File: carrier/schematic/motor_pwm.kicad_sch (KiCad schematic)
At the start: 9 parts, among them J36001 HX PZ2.54-3x8P ZZ, U36001 SN74HCT245PWR, U36003 SY6280AAC

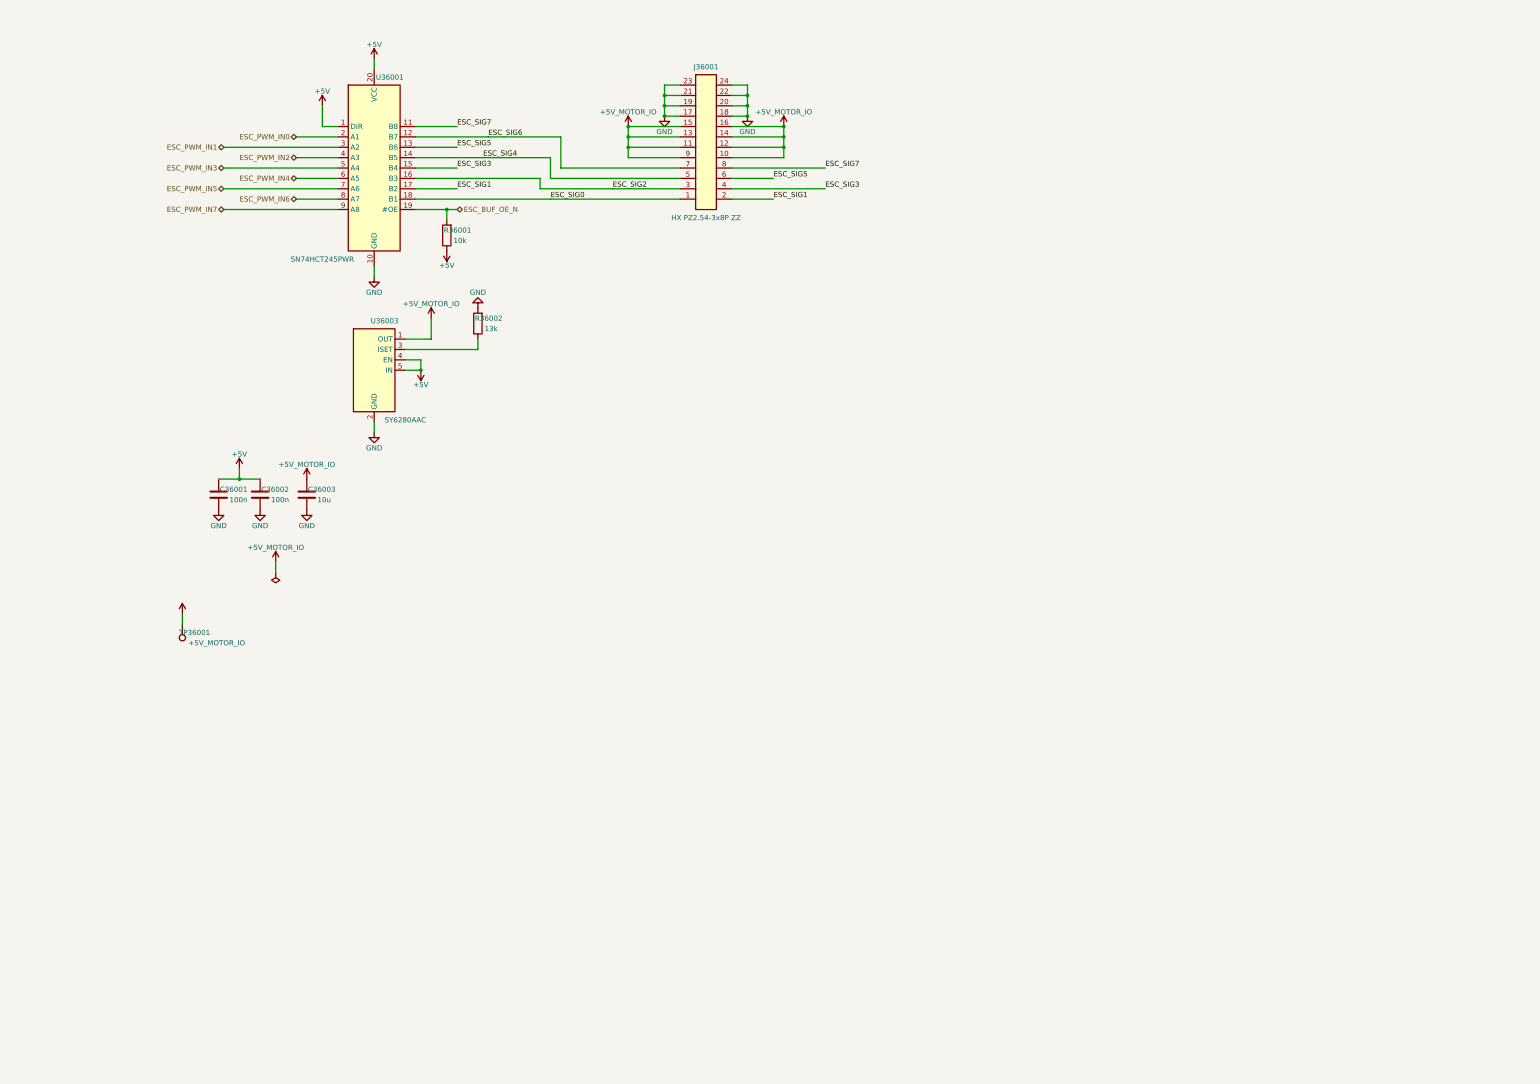
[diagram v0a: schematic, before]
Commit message: feat(motor_pwm LAW-7): instantiate the 33R output series-damping (placer row-wrap)
The 33R per-channel series damping on the 8 buffered ESC outputs was held back in
the prior commit (doc-tracked) because the part C25508 (4D03WGJ0330T5E 4x33R
array) is sourced but two 4-element arrays reconverging on the 24-pin header form
a tree the per-sheet chain placer strung to >400mm (over A3). LAW 7 says land a
sourced fix, not defer it — so this lands it:

 * motor_pwm.py: U1.B{i} -> RN(33R).in -> RN.out -> J1.SIG{1+i}; two isolated
   4D03 arrays (RN1 ch0-3, RN2 ch4-7), element j spanning pin (j+1)<->(8-j) per
   the footprint's vertical pad pairs. ISOLATED elements (no internal common) so
   a faulted ESC lead can't back-feed a sibling.
 * place.py: a within-component ROW-WRAP in _chain_template (PAPER_W_BUDGET=330).
   The discriminator is the POST-placement anchor (ax - row_left), NOT the prior
   attempt's pre-placement run-width that wrongly tripped lcd. Instrumented:
   widest FITTING sheet = lcd 292.7mm, overflowing motor_pwm = 370.1mm, so 330
   is a clean separator -> ONLY motor_pwm wraps. Proven byte-identical: of all 37
   sheets only motor_pwm.kicad_sch changed (lcd/hdmi_rx/all others identical).

The wrap demotes the crossed channel to labeled stubs (KiCad merges by name,
netlist untouched). BOARD PASS (159x145mm, 561 fp), DRC 0, LINK 0, CC-gate 0
shorts/0 opens, ratsnest/spacing/power-tree green; motor_pwm 8 local tests pass.
Only the 5V-rated output ESD array remains deferred (API-blocked — a 3.3V array
would clamp the 5V PWM).

Co-Authored-By: Claude Opus 4.8 <noreply@anthropic.com>
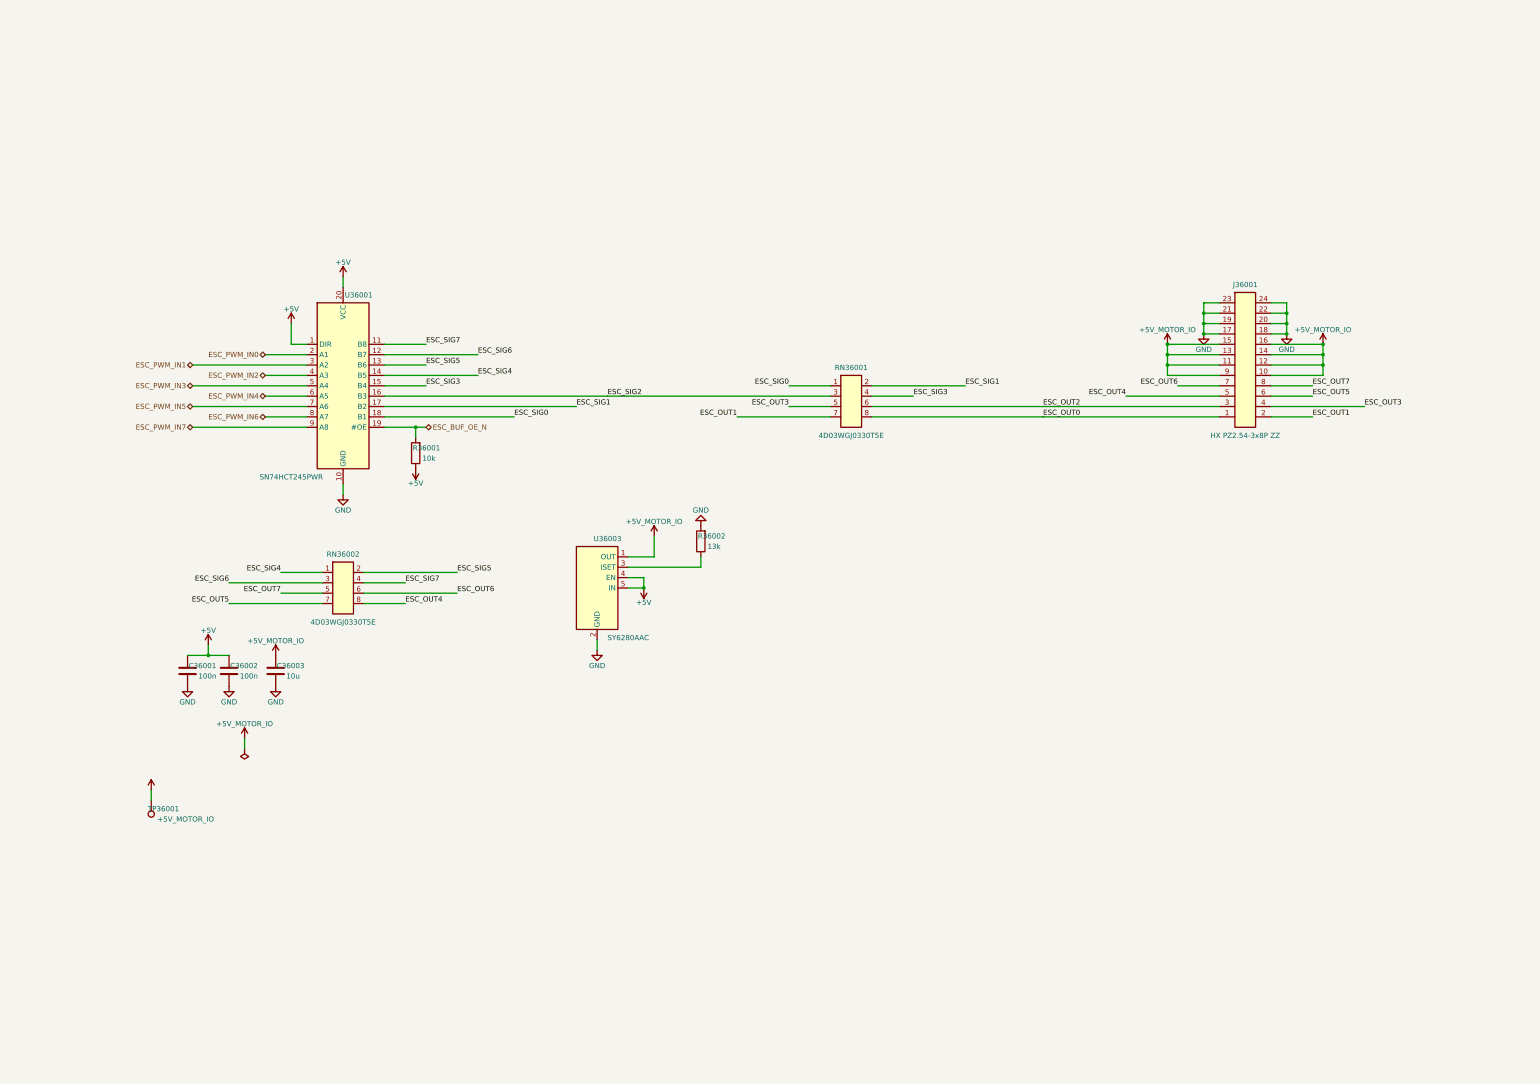
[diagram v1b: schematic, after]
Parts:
- added C36003: 10u, Capacitor_SMD:C_0805_2012Metric, symbol Device:C
- added TP36001: +5V_MOTOR_IO, TestPoint:TestPoint_Pad_D1.5mm, symbol Connector:TestPoint
- C36001: renamed from C36003; value 10u -> 100n; footprint Capacitor_SMD:C_0805_2012Metric -> Capacitor_SMD:C_0603_1608Metric; LCSC C15850 -> C14663
- C36002: renamed from TP36001; value +5V_MOTOR_IO -> 100n; footprint TestPoint:TestPoint_Pad_D1.5mm -> Capacitor_SMD:C_0603_1608Metric; symbol Connector:TestPoint -> Device:C; BOM exclude -> (none); LCSC (none) -> C14663
- J36001: renamed from U36003; value SY6280AAC -> HX PZ2.54-3x8P ZZ; footprint SY6280AAC:SY6280AAC -> HX_PZ2.54-3x8P_ZZ:HX_PZ2.54-3x8P_ZZ; symbol SY6280AAC:SY6280AAC -> HX_PZ2.54-3x8P_ZZ:HX_PZ2.54-3x8P_ZZ; LCSC C55136 -> C32713295
- R36002: renamed from C36002; value 100n -> 13k; footprint Capacitor_SMD:C_0603_1608Metric -> Resistor_SMD:R_0603_1608Metric; symbol Device:C -> Device:R; LCSC C14663 -> C22797
- RN36001: renamed from J36001; value HX PZ2.54-3x8P ZZ -> 4D03WGJ0330T5E; footprint HX_PZ2.54-3x8P_ZZ:HX_PZ2.54-3x8P_ZZ -> 4D03WGJ0330T5E:4D03WGJ0330T5E; symbol HX_PZ2.54-3x8P_ZZ:HX_PZ2.54-3x8P_ZZ -> 4D03WGJ0330T5E:4D03WGJ0330T5E; LCSC C32713295 -> C25508
- RN36002: renamed from R36002; value 13k -> 4D03WGJ0330T5E; footprint Resistor_SMD:R_0603_1608Metric -> 4D03WGJ0330T5E:4D03WGJ0330T5E; symbol Device:R -> 4D03WGJ0330T5E:4D03WGJ0330T5E; LCSC C22797 -> C25508
- U36003: renamed from C36001; value 100n -> SY6280AAC; footprint Capacitor_SMD:C_0603_1608Metric -> SY6280AAC:SY6280AAC; symbol Device:C -> SY6280AAC:SY6280AAC; LCSC C14663 -> C55136
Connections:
- net +5V: now also C36001.1, C36002.1, U36003.4 (EN), U36003.5 (IN); no longer J36001.4 (EN), J36001.5 (IN), R36002.1, U36003.1
- net +5V_MOTOR_IO: now also J36001.10, J36001.11, J36001.12, J36001.13, J36001.14, J36001.15, J36001.16, J36001.9, U36003.1 (OUT), C36003.1, TP36001.1; no longer C36001.1, C36002.1, J36001.1 (OUT), RN36001.10, RN36001.11, RN36001.12, RN36001.13, RN36001.14, RN36001.15, RN36001.16, RN36001.9
- net ESC_SIG4: now also RN36002.1; no longer RN36001.5
- net ESC_SIG5: now also RN36002.2; no longer RN36001.6
- net ESC_SIG6: now also RN36002.3; no longer RN36001.7
- net ESC_SIG7: now also RN36002.4; no longer RN36001.8
- net GND: now also C36002.2, J36001.17, J36001.18, J36001.19, J36001.20, J36001.21, J36001.22, J36001.23, J36001.24, C36003.2; no longer J36001.2 (GND), RN36001.17, RN36001.18, RN36001.19, RN36001.20, RN36001.21, RN36001.22, RN36001.23, RN36001.24, RN36002.2
- net ESC_OUT2: now reaches J36001.3
- net ESC_OUT2: now also RN36001.6; no longer RN36002.1
- new net: R36002.1, U36003.3 (ISET)
- new net ESC_OUT0: J36001.1, RN36001.8
- new net ESC_OUT1: J36001.2, RN36001.7
- new net ESC_OUT3: J36001.4, RN36001.5
- new net ESC_OUT4: J36001.5, RN36002.8
- new net ESC_OUT5: J36001.6, RN36002.7
- new net ESC_OUT6: J36001.7, RN36002.6
- new net ESC_OUT7: J36001.8, RN36002.5
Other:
- moved on the sheet: C36001, R36001, U36001

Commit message: feat(motor_pwm OPEN-3a): 5V-rated ESD on the 8 off-board PWM outputs
Lands the long-deferred output ESD — NO EasyEDA CAD API needed (it was rate-
limited): SRV05-4 is a jellybean part with a STOCK KiCad symbol
(Power_Protection:SRV05-4, pinout built-in) + stock SOT-23-6 footprint; the
verified LCSC C2836319 (MSKSEMI SRV05-4, 375k stock) rides in the value + a
ratings.py line.

Two arrays clamp ESC_OUT0..7 to +5V/GND right at the connector, ahead of the 33R
+ buffer. SRV05-4 is 5V-line rated, so unlike the spec's 3.3V PESD3V3L4UG it does
NOT clamp the 5V buffered signals. Bound by pad NUMBER (schgen resolves pins by
number): IO1=1/VN=2/IO2=3/IO3=4/VP=5/IO4=6 -> VP->+5V, VN->GND, the 4 I/O ->
4 channels each. The taps distribute across 8 separate ESC_OUT nets, so (unlike
the motor_sense bulk cap on one dense net) the schematic router took it with no
congestion. D36001/D36002 placed clean below the buffer (render-verified, refs
0-overlap per the LAW-1 gate).

PART RULES PASS (C2836319 = diode v_max 5.0), DRC 0, 564 footprints, motor_pwm
8 tests + full suite 662 passed. OPEN-3: (a) ESD + (b) bulk cap now both landed;
(c) shunt remains a design decision (aggregate-current sizing + INA range).

Co-Authored-By: Claude Opus 4.8 <noreply@anthropic.com>
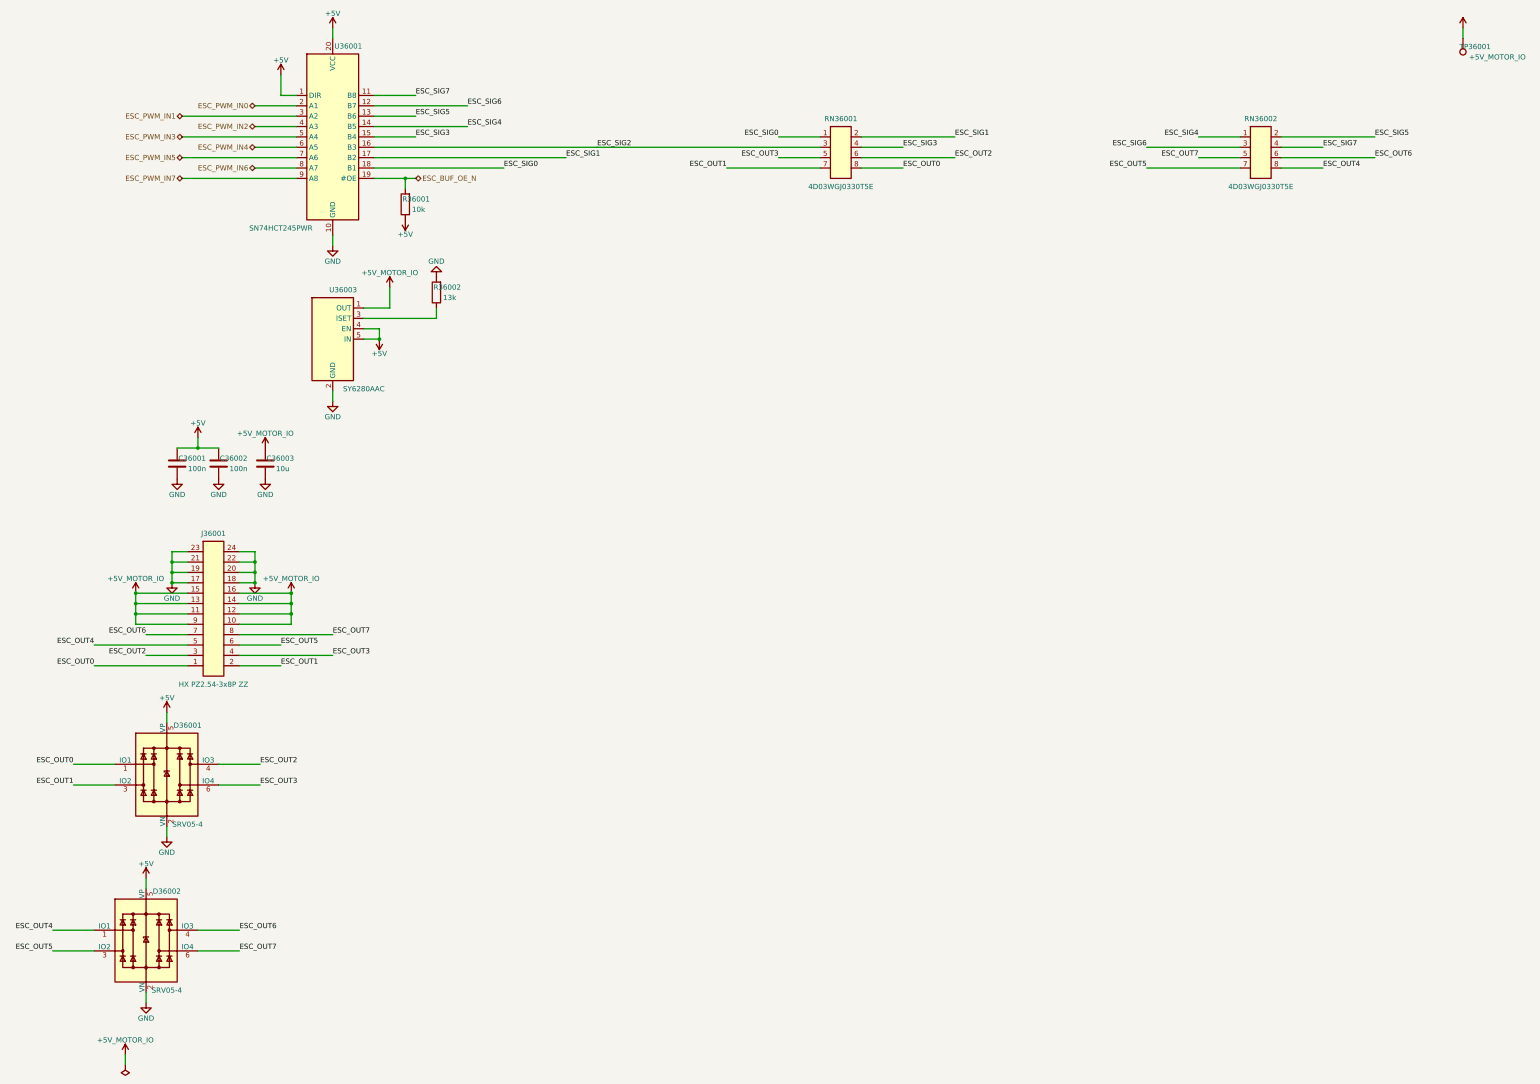
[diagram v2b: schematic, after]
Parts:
- added D36002: SRV05-4, Package_TO_SOT_SMD:SOT-23-6, symbol Power_Protection:SRV05-4
- added TP36001: +5V_MOTOR_IO, TestPoint:TestPoint_Pad_D1.5mm, symbol Connector:TestPoint
- C36001: renamed from R36002; value 13k -> 100n; footprint Resistor_SMD:R_0603_1608Metric -> Capacitor_SMD:C_0603_1608Metric; symbol Device:R -> Device:C; LCSC C22797 -> C14663
- C36003: renamed from C36002; value 100n -> 10u; footprint Capacitor_SMD:C_0603_1608Metric -> Capacitor_SMD:C_0805_2012Metric; LCSC C14663 -> C15850
- D36001: renamed from TP36001; value +5V_MOTOR_IO -> SRV05-4; footprint TestPoint:TestPoint_Pad_D1.5mm -> Package_TO_SOT_SMD:SOT-23-6; symbol Connector:TestPoint -> Power_Protection:SRV05-4; BOM exclude -> (none); LCSC (none) -> C2836319
- J36001: renamed from C36003; value 10u -> HX PZ2.54-3x8P ZZ; footprint Capacitor_SMD:C_0805_2012Metric -> HX_PZ2.54-3x8P_ZZ:HX_PZ2.54-3x8P_ZZ; symbol Device:C -> HX_PZ2.54-3x8P_ZZ:HX_PZ2.54-3x8P_ZZ; LCSC C15850 -> C32713295
- R36002: renamed from U36003; value SY6280AAC -> 13k; footprint SY6280AAC:SY6280AAC -> Resistor_SMD:R_0603_1608Metric; symbol SY6280AAC:SY6280AAC -> Device:R; LCSC C55136 -> C22797
- RN36002: renamed from J36001; value HX PZ2.54-3x8P ZZ -> 4D03WGJ0330T5E; footprint HX_PZ2.54-3x8P_ZZ:HX_PZ2.54-3x8P_ZZ -> 4D03WGJ0330T5E:4D03WGJ0330T5E; symbol HX_PZ2.54-3x8P_ZZ:HX_PZ2.54-3x8P_ZZ -> 4D03WGJ0330T5E:4D03WGJ0330T5E; LCSC C32713295 -> C25508
- U36003: renamed from RN36002; value 4D03WGJ0330T5E -> SY6280AAC; footprint 4D03WGJ0330T5E:4D03WGJ0330T5E -> SY6280AAC:SY6280AAC; symbol 4D03WGJ0330T5E:4D03WGJ0330T5E -> SY6280AAC:SY6280AAC; LCSC C25508 -> C55136
- renumbered C36001 to C36002
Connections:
- net +5V: now also C36001.1, D36001.5 (VP), U36003.4 (EN), U36003.5 (IN), D36002.5 (VP); no longer C36003.1, R36002.4 (EN), R36002.5 (IN)
- net +5V_MOTOR_IO: now also C36003.1, J36001.10, J36001.11, J36001.12, J36001.13, J36001.14, J36001.15, J36001.16, J36001.9, U36003.1 (OUT), TP36001.1; no longer D36001.1, J36001.1, R36002.1 (OUT), RN36002.10, RN36002.11, RN36002.12, RN36002.13, RN36002.14, RN36002.15, RN36002.16, RN36002.9
- net ESC_OUT0: now also D36001.1 (IO1), J36001.1; no longer RN36002.1
- net ESC_OUT1: now also D36001.3 (IO2), J36001.2; no longer RN36002.2
- net ESC_OUT2: now also D36001.4 (IO3), J36001.3; no longer RN36002.3
- net ESC_OUT3: now also D36001.6 (IO4), J36001.4; no longer RN36002.4
- net ESC_OUT4: now also J36001.5, RN36002.8, D36002.1 (IO1); no longer RN36002.5, U36003.8
- net ESC_OUT5: now also J36001.6, RN36002.7, D36002.3 (IO2); no longer RN36002.6, U36003.7
- net ESC_OUT6: now also J36001.7, RN36002.6, D36002.4 (IO3); no longer RN36002.7, U36003.6
- net ESC_OUT7: now also J36001.8, RN36002.5, D36002.6 (IO4); no longer RN36002.8, U36003.5
- net ESC_SIG4: now also RN36002.1; no longer U36003.1
- net ESC_SIG5: now also RN36002.2; no longer U36003.2
- net ESC_SIG6: now also RN36002.3; no longer U36003.3
- net ESC_SIG7: now also RN36002.4; no longer U36003.4
- net GND: now also D36001.2 (VN), J36001.17, J36001.18, J36001.19, J36001.20, J36001.21, J36001.22, J36001.23, J36001.24, U36003.2 (GND), D36002.2 (VN); no longer J36001.2, RN36002.17, RN36002.18, RN36002.19, RN36002.20, RN36002.21, RN36002.22, RN36002.23, RN36002.24
- new net: R36002.1, U36003.3 (ISET)
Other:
- moved on the sheet: C36002, C36003, R36001, RN36001, U36001
